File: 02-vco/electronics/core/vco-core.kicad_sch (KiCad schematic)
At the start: 2 parts, among them J3 Conn_02x05_Odd_Even, J4 Conn_01x04

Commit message: Designed VCO core PCB
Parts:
- added H1, H2, H3, H4: MountingHole, MountingHole:MountingHole_3.2mm_M3_DIN965_Pad, symbol Mechanical:MountingHole
- J1: renamed from J4; footprint (none) -> Connector_PinSocket_2.54mm:PinSocket_1x04_P2.54mm_Vertical
- J2: renamed from J3; footprint (none) -> Connector_PinSocket_2.54mm:PinSocket_2x05_P2.54mm_Vertical
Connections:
- net FM: now also J1.3 (Pin_3); no longer J1.2 (Pin_2)
- net HARD_SYNC: now also J1.2 (Pin_2); no longer J1.3 (Pin_3)
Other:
- sheet Raw saw renamed Raw oscillator
- sheet Raw oscillator: file sheets/raw-saw.kicad_sch -> sheets/raw-oscillator.kicad_sch

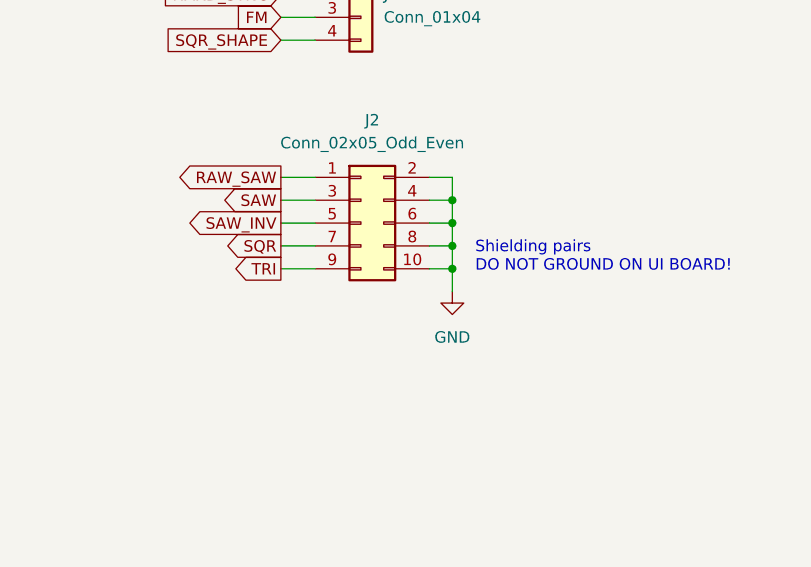
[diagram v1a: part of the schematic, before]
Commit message: Added whaveshapers to VCO PCB
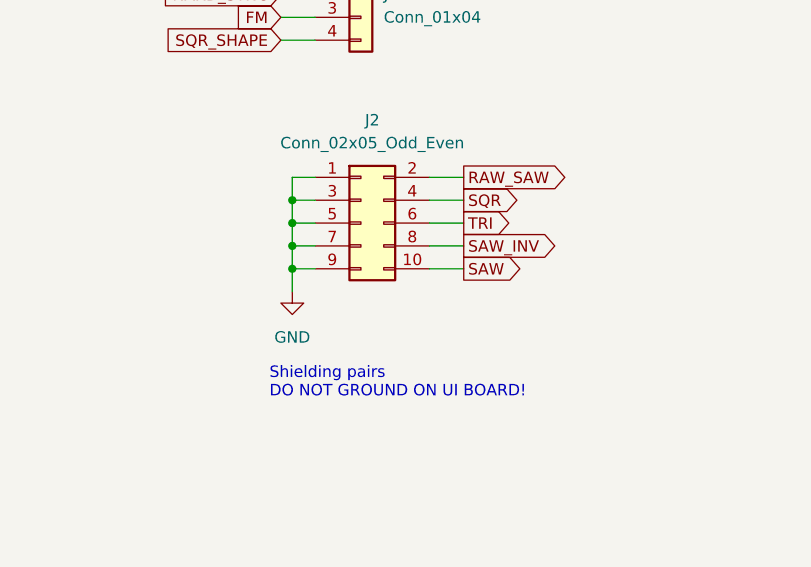
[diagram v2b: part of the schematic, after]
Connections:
- net GND: now also J2.1 (Pin_1), J2.3 (Pin_3), J2.5 (Pin_5), J2.7 (Pin_7), J2.9 (Pin_9); no longer J2.10 (Pin_10), J2.2 (Pin_2), J2.4 (Pin_4), J2.6 (Pin_6), J2.8 (Pin_8)
- net RAW_SAW: now also J2.2 (Pin_2); no longer J2.1 (Pin_1)
- net SAW: now also J2.10 (Pin_10); no longer J2.3 (Pin_3)
- net SAW_INV: now also J2.8 (Pin_8); no longer J2.5 (Pin_5)
- net SQR: now also J2.4 (Pin_4); no longer J2.7 (Pin_7)
- net TRI: now also J2.6 (Pin_6); no longer J2.9 (Pin_9)
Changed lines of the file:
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@@
 	(text "Shielding pairs\nDO NOT GROUND ON UI BOARD!"
 		(exclude_from_sim no)
-		(at 228.6 110.49 0)
+		(at 205.74 124.46 0)
 		(effects
 			(font
@@
 	)
 	(junction
-		(at 226.06 109.22)
+		(at 208.28 109.22)
 		(diameter 0)
 		(color 0 0 0 0)
 	)
 	(junction
-		(at 226.06 106.68)
+		(at 208.28 106.68)
 		(diameter 0)
 		(color 0 0 0 0)
 	)
 	(junction
-		(at 226.06 104.14)
+		(at 208.28 104.14)
 		(diameter 0)
 		(color 0 0 0 0)
 	)
 	(junction
-		(at 226.06 111.76)
+		(at 208.28 111.76)
 		(diameter 0)
 		(color 0 0 0 0)
@@
 	(wire
 		(pts
-			(xy 226.06 109.22) (xy 226.06 111.76)
+			(xy 208.28 109.22) (xy 208.28 111.76)
 		)
 		(stroke
@@
 	(wire
 		(pts
-			(xy 207.01 111.76) (xy 210.82 111.76)
-		)
-		(stroke
-			(width 0)
-			(type default)
-		)
-	)
-	(wire
-		(pts
-			(xy 223.52 111.76) (xy 226.06 111.76)
-		)
-		(stroke
-			(width 0)
-			(type default)
-		)
-	)
-	(wire
-		(pts
-			(xy 223.52 104.14) (xy 226.06 104.14)
+			(xy 227.33 111.76) (xy 223.52 111.76)
+		)
+		(stroke
+			(width 0)
+			(type default)
+		)
+	)
+	(wire
+		(pts
+			(xy 210.82 111.76) (xy 208.28 111.76)
+		)
+		(stroke
+			(width 0)
+			(type default)
+		)
+	)
+	(wire
+		(pts
+			(xy 210.82 104.14) (xy 208.28 104.14)
 		)
 		(stroke
@@
 	(wire
 		(pts
-			(xy 226.06 101.6) (xy 226.06 104.14)
-		)
-		(stroke
-			(width 0)
-			(type default)
-		)
-	)
-	(wire
-		(pts
-			(xy 226.06 106.68) (xy 226.06 109.22)
-		)
-		(stroke
-			(width 0)
-			(type default)
-		)
-	)
-	(wire
-		(pts
-			(xy 207.01 106.68) (xy 210.82 106.68)
-		)
-		(stroke
-			(width 0)
-			(type default)
-		)
-	)
-	(wire
-		(pts
-			(xy 207.01 101.6) (xy 210.82 101.6)
-		)
-		(stroke
-			(width 0)
-			(type default)
-		)
-	)
-	(wire
-		(pts
-			(xy 207.01 109.22) (xy 210.82 109.22)
+			(xy 208.28 101.6) (xy 208.28 104.14)
+		)
+		(stroke
+			(width 0)
+			(type default)
+		)
+	)
+	(wire
+		(pts
+			(xy 208.28 106.68) (xy 208.28 109.22)
+		)
+		(stroke
+			(width 0)
+			(type default)
+		)
+	)
+	(wire
+		(pts
+			(xy 227.33 106.68) (xy 223.52 106.68)
+		)
+		(stroke
+			(width 0)
+			(type default)
+		)
+	)
+	(wire
+		(pts
+			(xy 227.33 101.6) (xy 223.52 101.6)
+		)
+		(stroke
+			(width 0)
+			(type default)
+		)
+	)
+	(wire
+		(pts
+			(xy 227.33 109.22) (xy 223.52 109.22)
 		)
 		(stroke
@@
 	(wire
 		(pts
-			(xy 223.52 101.6) (xy 226.06 101.6)
+			(xy 210.82 101.6) (xy 208.28 101.6)
 		)
 		(stroke
@@
 	(wire
 		(pts
-			(xy 223.52 109.22) (xy 226.06 109.22)
-		)
-		(stroke
-			(width 0)
-			(type default)
-		)
-	)
-	(wire
-		(pts
-			(xy 226.06 104.14) (xy 226.06 106.68)
-		)
-		(stroke
-			(width 0)
-			(type default)
-		)
-	)
-	(wire
-		(pts
-			(xy 226.06 111.76) (xy 226.06 114.3)
+			(xy 210.82 109.22) (xy 208.28 109.22)
+		)
+		(stroke
+			(width 0)
+			(type default)
+		)
+	)
+	(wire
+		(pts
+			(xy 208.28 104.14) (xy 208.28 106.68)
+		)
+		(stroke
+			(width 0)
+			(type default)
+		)
+	)
+	(wire
+		(pts
+			(xy 208.28 111.76) (xy 208.28 114.3)
 		)
 		(stroke
@@
 	(wire
 		(pts
-			(xy 223.52 106.68) (xy 226.06 106.68)
+			(xy 210.82 106.68) (xy 208.28 106.68)
 		)
 		(stroke
@@
 	(wire
 		(pts
-			(xy 207.01 104.14) (xy 210.82 104.14)
+			(xy 227.33 104.14) (xy 223.52 104.14)
 		)
 		(stroke
@@
 	(global_label "SQR"
 		(shape output)
-		(at 207.01 109.22 180)
-		(fields_autoplaced yes)
-		(effects
-			(font
-				(size 1.27 1.27)
-			)
-			(justify right)
-		)
-		(property "Intersheetrefs" "${INTERSHEET_REFS}"
-			(at 200.2148 109.22 0)
-			(effects
-				(font
-					(size 1.27 1.27)
-				)
-				(justify right)
+		(at 227.33 104.14 0)
+		(fields_autoplaced yes)
+		(effects
+			(font
+				(size 1.27 1.27)
+			)
+			(justify left)
+		)
+		(property "Intersheetrefs" "${INTERSHEET_REFS}"
+			(at 234.1252 104.14 0)
+			(effects
+				(font
+					(size 1.27 1.27)
+				)
+				(justify left)
 				(hide yes)
 			)
@@
 	(global_label "SAW_INV"
 		(shape output)
-		(at 207.01 106.68 180)
-		(fields_autoplaced yes)
-		(effects
-			(font
-				(size 1.27 1.27)
-			)
-			(justify right)
-		)
-		(property "Intersheetrefs" "${INTERSHEET_REFS}"
-			(at 196.2838 106.68 0)
-			(effects
-				(font
-					(size 1.27 1.27)
-				)
-				(justify right)
+		(at 227.33 109.22 0)
+		(fields_autoplaced yes)
+		(effects
+			(font
+				(size 1.27 1.27)
+			)
+			(justify left)
+		)
+		(property "Intersheetrefs" "${INTERSHEET_REFS}"
+			(at 238.0562 109.22 0)
+			(effects
+				(font
+					(size 1.27 1.27)
+				)
+				(justify left)
 				(hide yes)
 			)
@@
 	(global_label "SAW"
 		(shape output)
-		(at 207.01 104.14 180)
-		(fields_autoplaced yes)
-		(effects
-			(font
-				(size 1.27 1.27)
-			)
-			(justify right)
-		)
-		(property "Intersheetrefs" "${INTERSHEET_REFS}"
-			(at 200.2753 104.14 0)
-			(effects
-				(font
-					(size 1.27 1.27)
-				)
-				(justify right)
+		(at 227.33 111.76 0)
+		(fields_autoplaced yes)
+		(effects
+			(font
+				(size 1.27 1.27)
+			)
+			(justify left)
+		)
+		(property "Intersheetrefs" "${INTERSHEET_REFS}"
+			(at 234.0647 111.76 0)
+			(effects
+				(font
+					(size 1.27 1.27)
+				)
+				(justify left)
 				(hide yes)
 			)
@@
 	(global_label "RAW_SAW"
 		(shape output)
-		(at 207.01 101.6 180)
-		(fields_autoplaced yes)
-		(effects
-			(font
-				(size 1.27 1.27)
-			)
-			(justify right)
-		)
-		(property "Intersheetrefs" "${INTERSHEET_REFS}"
-			(at 195.4977 101.6 0)
-			(effects
-				(font
-					(size 1.27 1.27)
-				)
-				(justify right)
+		(at 227.33 101.6 0)
+		(fields_autoplaced yes)
+		(effects
+			(font
+				(size 1.27 1.27)
+			)
+			(justify left)
+		)
+		(property "Intersheetrefs" "${INTERSHEET_REFS}"
+			(at 238.8423 101.6 0)
+			(effects
+				(font
+					(size 1.27 1.27)
+				)
+				(justify left)
 				(hide yes)
 			)
@@
 	(global_label "TRI"
 		(shape output)
-		(at 207.01 111.76 180)
-		(fields_autoplaced yes)
-		(effects
-			(font
-				(size 1.27 1.27)
-			)
-			(justify right)
-		)
-		(property "Intersheetrefs" "${INTERSHEET_REFS}"
-			(at 201.1824 111.76 0)
-			(effects
-				(font
-					(size 1.27 1.27)
-				)
-				(justify right)
+		(at 227.33 106.68 0)
+		(fields_autoplaced yes)
+		(effects
+			(font
+				(size 1.27 1.27)
+			)
+			(justify left)
+		)
+		(property "Intersheetrefs" "${INTERSHEET_REFS}"
+			(at 233.1576 106.68 0)
+			(effects
+				(font
+					(size 1.27 1.27)
+				)
+				(justify left)
 				(hide yes)
 			)
@@
 	(symbol
 		(lib_id "power:GND")
-		(at 226.06 114.3 0)
+		(at 208.28 114.3 0)
+		(mirror y)
 		(unit 1)
 		(exclude_from_sim no)
@@
 		(fields_autoplaced yes)
 		(property "Reference" "#PWR01"
-			(at 226.06 120.65 0)
+			(at 208.28 120.65 0)
 			(effects
 				(font
@@
 		)
 		(property "Value" "GND"
-			(at 226.06 119.38 0)
+			(at 208.28 119.38 0)
 			(effects
 				(font
@@
 		)
 		(property "Footprint" ""
-			(at 226.06 114.3 0)
+			(at 208.28 114.3 0)
 			(effects
 				(font
@@
 		)
 		(property "Datasheet" ""
-			(at 226.06 114.3 0)
+			(at 208.28 114.3 0)
 			(effects
 				(font
@@
 		)
 		(property "Description" "Power symbol creates a global label with name \"GND\" , ground"
-			(at 226.06 114.3 0)
-			(effects
-				(font
+			(at 208.28 114.3 0)
+			(effects
+				(font

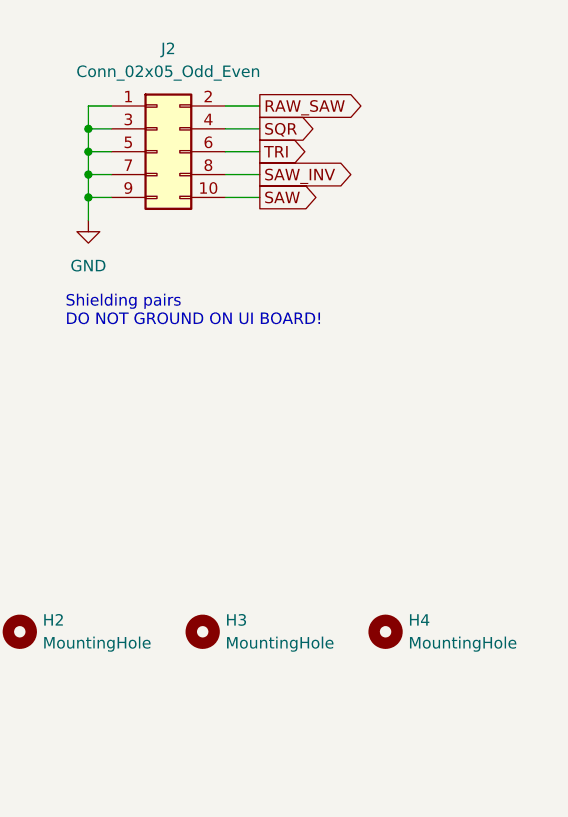
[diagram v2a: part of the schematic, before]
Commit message: Shrink PCB
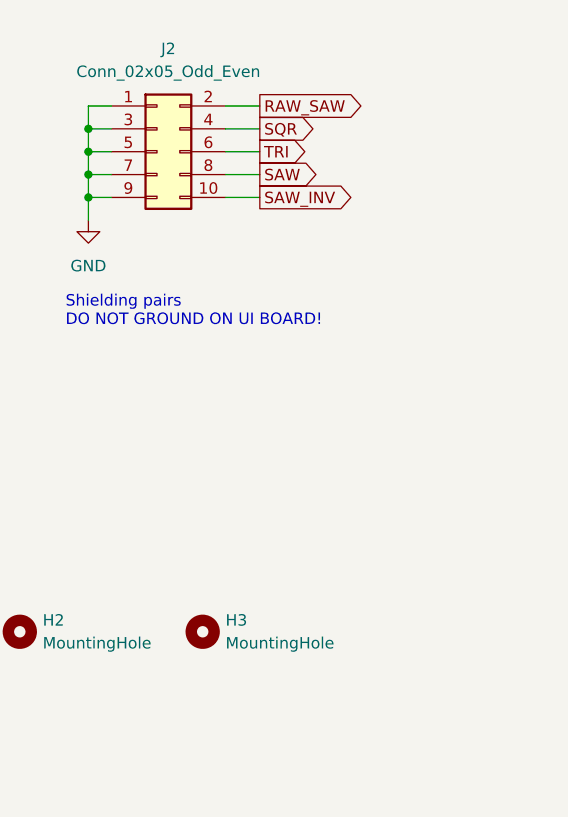
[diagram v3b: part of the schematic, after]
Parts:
- removed H4: MountingHole, MountingHole:MountingHole_3.2mm_M3_DIN965_Pad, symbol Mechanical:MountingHole
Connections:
- net SAW: now also J2.8 (Pin_8); no longer J2.10 (Pin_10)
- net SAW_INV: now also J2.10 (Pin_10); no longer J2.8 (Pin_8)
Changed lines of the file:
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@@
 	(global_label "SAW_INV"
 		(shape output)
-		(at 227.33 109.22 0)
+		(at 227.33 111.76 0)
 		(fields_autoplaced yes)
 		(effects
@@
 		)
 		(property "Intersheetrefs" "${INTERSHEET_REFS}"
-			(at 238.0562 109.22 0)
+			(at 238.0562 111.76 0)
 			(effects
 				(font
@@
 	(global_label "SAW"
 		(shape output)
-		(at 227.33 111.76 0)
+		(at 227.33 109.22 0)
 		(fields_autoplaced yes)
 		(effects
@@
 		)
 		(property "Intersheetrefs" "${INTERSHEET_REFS}"
-			(at 234.0647 111.76 0)
+			(at 234.0647 109.22 0)
 			(effects
 				(font
@@
 					(unit 1)
 				)
-			)
-		)
-	)
-	(symbol
-		(lib_id "Mechanical:MountingHole")
-		(at 241.3 160.02 0)
-		(unit 1)
-		(exclude_from_sim no)
-		(in_bom no)
-		(on_board yes)
-		(dnp no)
-		(fields_autoplaced yes)
-		(property "Reference" "H4"
-			(at 243.84 158.7499 0)
-			(effects
-				(font
-					(size 1.27 1.27)
-				)
-				(justify left)
-			)
-		)
-		(property "Value" "MountingHole"
-			(at 243.84 161.2899 0)
-			(effects
-				(font
-					(size 1.27 1.27)
-				)
-				(justify left)
-			)
-		)
-		(property "Footprint" "MountingHole:MountingHole_3.2mm_M3_DIN965_Pad"
-			(at 241.3 160.02 0)
-			(effects
-				(font
-					(size 1.27 1.27)
-				)
-				(hide yes)
-			)
-		)
-		(property "Datasheet" "~"
-			(at 241.3 160.02 0)
-			(effects
-				(font
-					(size 1.27 1.27)
-				)
-				(hide yes)
-			)
-		)
-		(property "Description" "Mounting Hole without connection"
-			(at 241.3 160.02 0)
-			(effects
-				(font
-					(size 1.27 1.27)
-				)
-				(hide yes)
-			)
-		)
-		(property "Part No." ""
-			(at 241.3 160.02 0)
-			(effects
-				(font
-					(size 1.27 1.27)
-				)
-				(hide yes)
-			)
-		)
-		(property "Part URL" ""
-			(at 241.3 160.02 0)
-			(effects
-				(font
-					(size 1.27 1.27)
-				)
-				(hide yes)
-			)
-		)
-		(property "Vendor" ""
-			(at 241.3 160.02 0)
-			(effects
-				(font
-					(size 1.27 1.27)
-				)
-				(hide yes)
-			)
-		)
-		(property "LCSC" ""
-			(at 241.3 160.02 0)
-			(effects
-				(font
-					(size 1.27 1.27)
-				)
-				(hide yes)
-			)
-		)
-		(instances
-			(project "vco-core"
-				(path "/8e2e31f3-eed5-4de1-966c-f4162758c735"
-					(reference "H4")
-					(unit 1)
-				)

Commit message: Cleanup
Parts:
- J1, J2: now left out of the parts list
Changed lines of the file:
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@@
 		(unit 1)
 		(exclude_from_sim no)
-		(in_bom yes)
+		(in_bom no)
 		(on_board yes)
 		(dnp no)
@@
 		(unit 1)
 		(exclude_from_sim no)
-		(in_bom yes)
+		(in_bom no)
 		(on_board yes)
 		(dnp no)

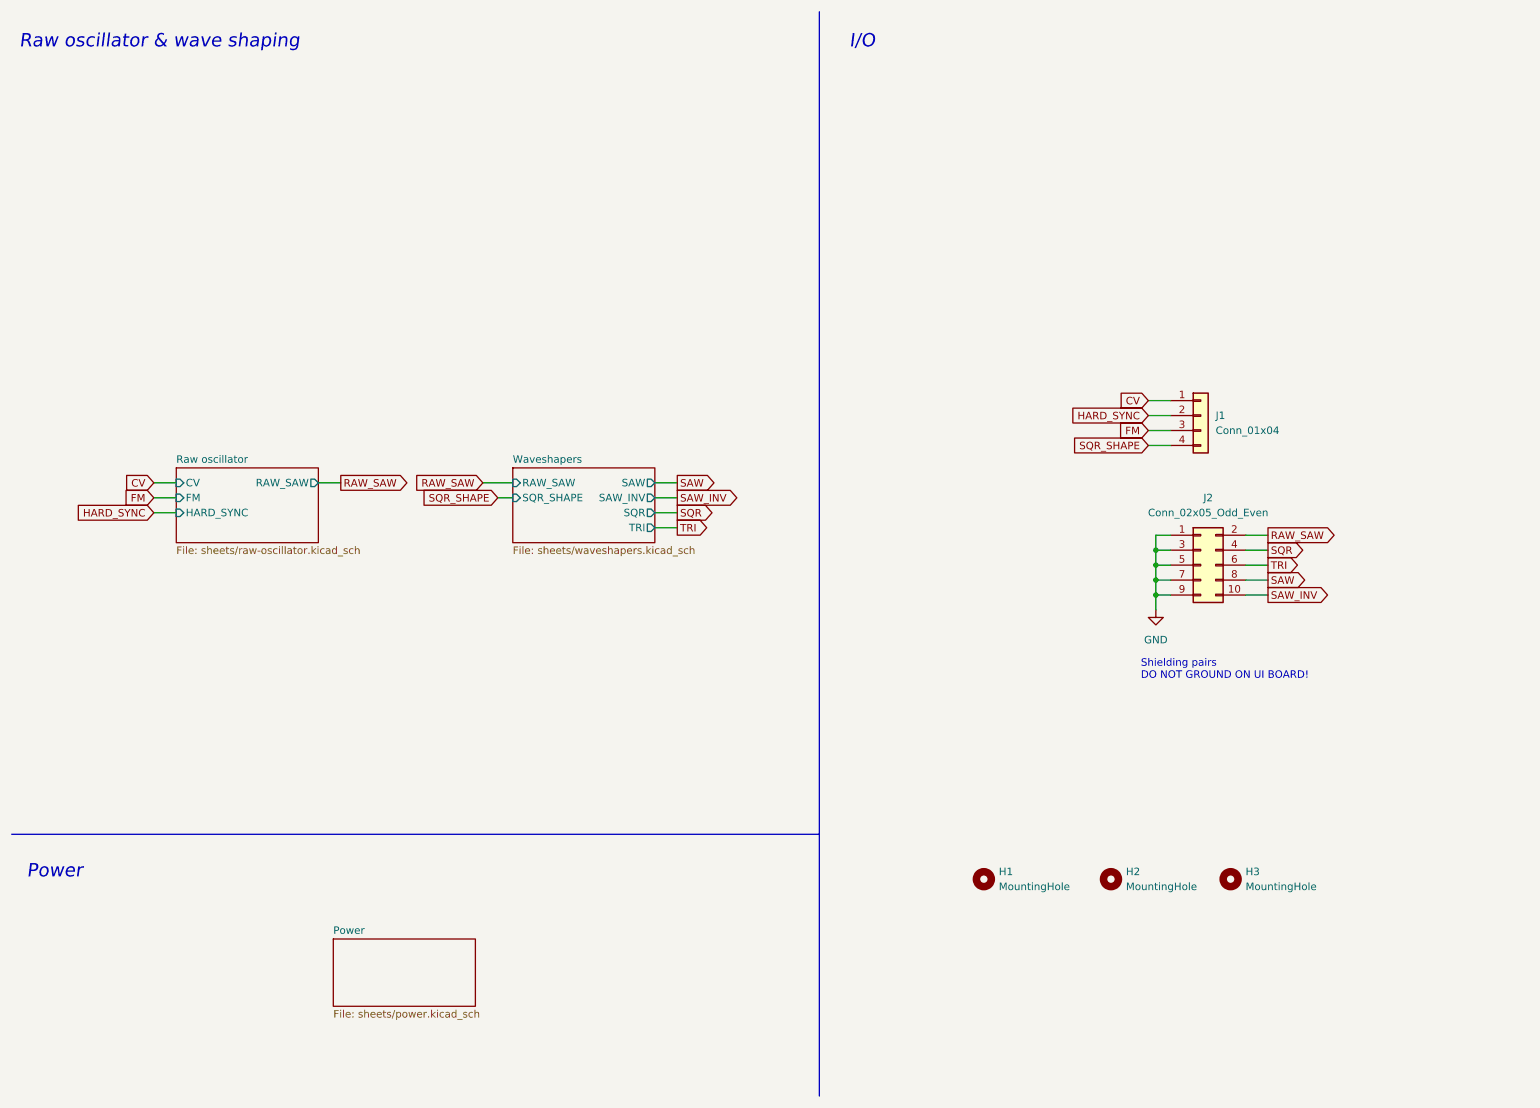
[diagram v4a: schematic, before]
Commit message: Added sub & noise circuit to VCO core
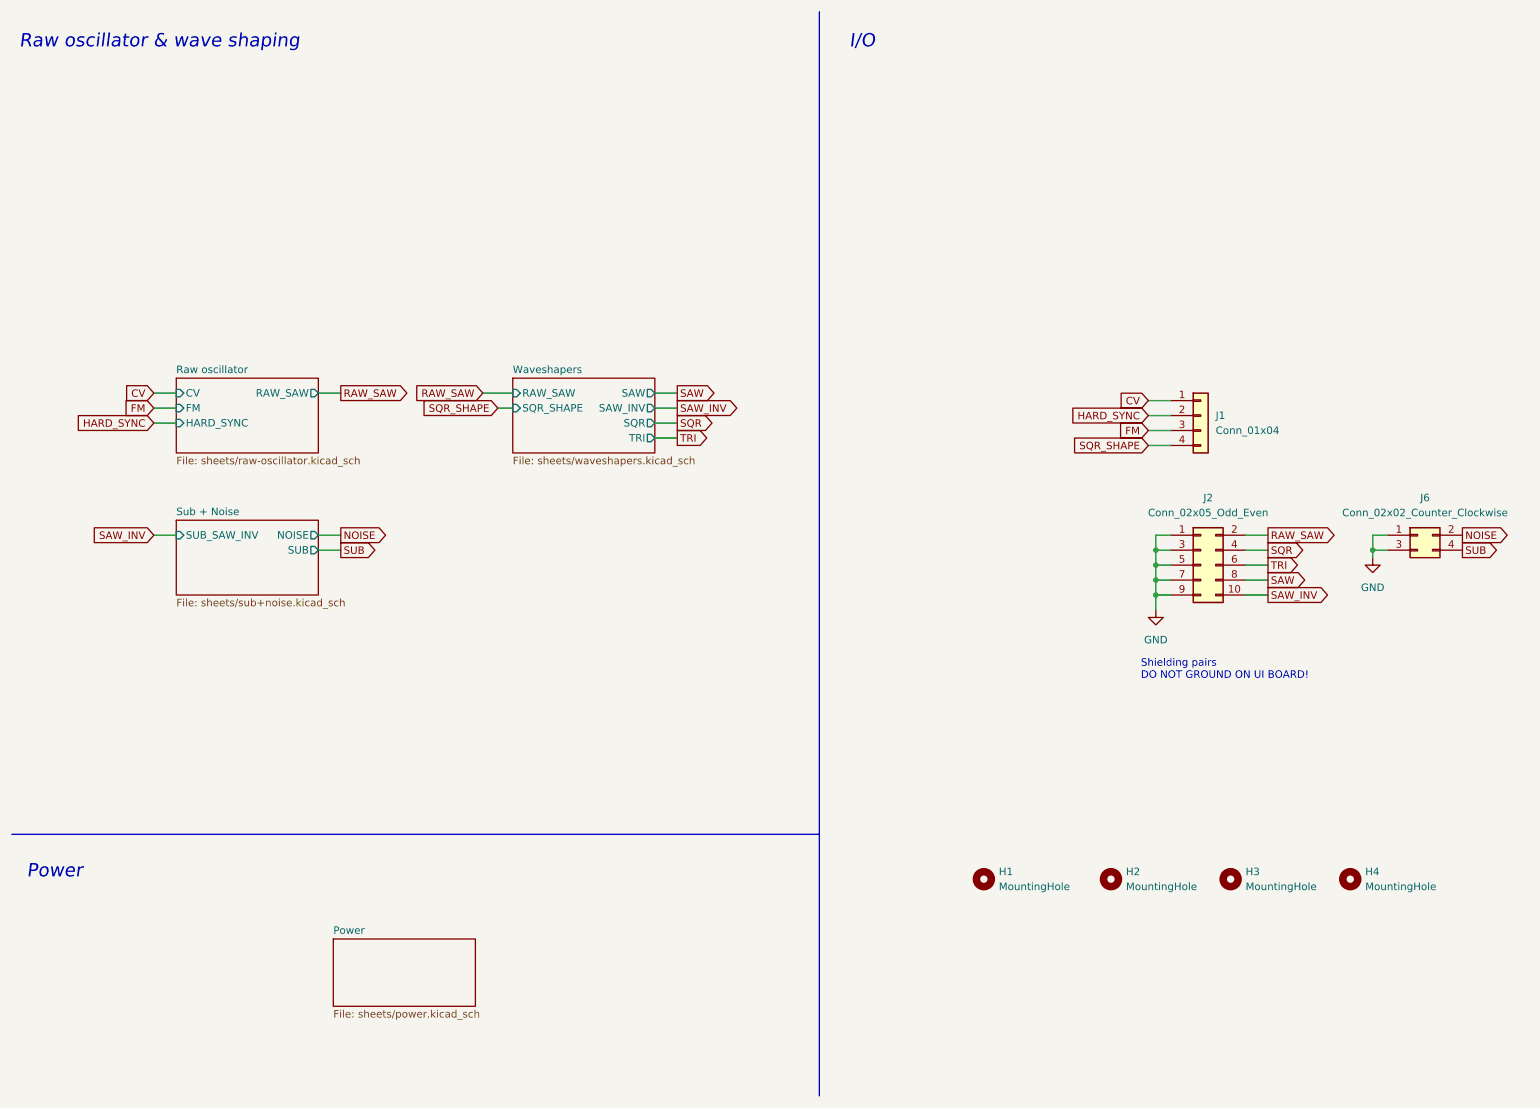
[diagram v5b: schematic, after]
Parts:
- added H4: MountingHole, MountingHole:MountingHole_3.2mm_M3_DIN965_Pad, symbol Mechanical:MountingHole
- added J6: Conn_02x02_Counter_Clockwise, Connector_PinSocket_2.54mm:PinSocket_2x02_P2.54mm_Vertical, symbol Connector_Generic:Conn_02x02_Odd_Even
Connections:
- net GND: now also J6.1 (Pin_1), J6.3 (Pin_3)
- new net NOISE: J6.2 (Pin_2)
- new net SUB: J6.4 (Pin_4)
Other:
- added sheet Sub + Noise (sheets/sub+noise.kicad_sch)

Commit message: Updated sub circuit
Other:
- sheet Sub + Noise ports: added SUB_SAW; removed SUB_SAW_INV
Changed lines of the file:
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@@
 		)
 	)
-	(global_label "SAW_INV"
+	(global_label "SAW"
 		(shape input)
 		(at 38.1 101.6 180)
@@
 		)
 		(property "Intersheetrefs" "${INTERSHEET_REFS}"
-			(at 27.3738 101.6 0)
+			(at 31.3653 101.6 0)
 			(effects
 				(font
@@
 			)
 		)
-		(pin "SUB_SAW_INV" input
+		(pin "SUB_SAW" input
 			(at 41.91 101.6 180)
 			(effects
